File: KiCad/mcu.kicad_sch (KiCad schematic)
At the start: 12 parts, among them U6 STM32G0B1RET6, U7 RN4871-I_RM128, Y1 32.768kHz, Y2 8MHz

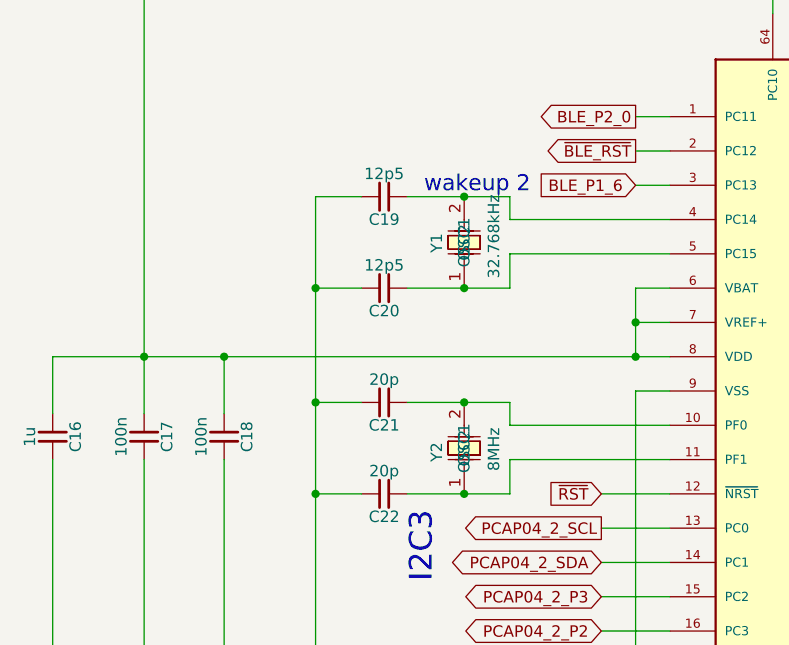
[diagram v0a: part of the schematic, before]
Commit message: crystal capacitors changed to correct values
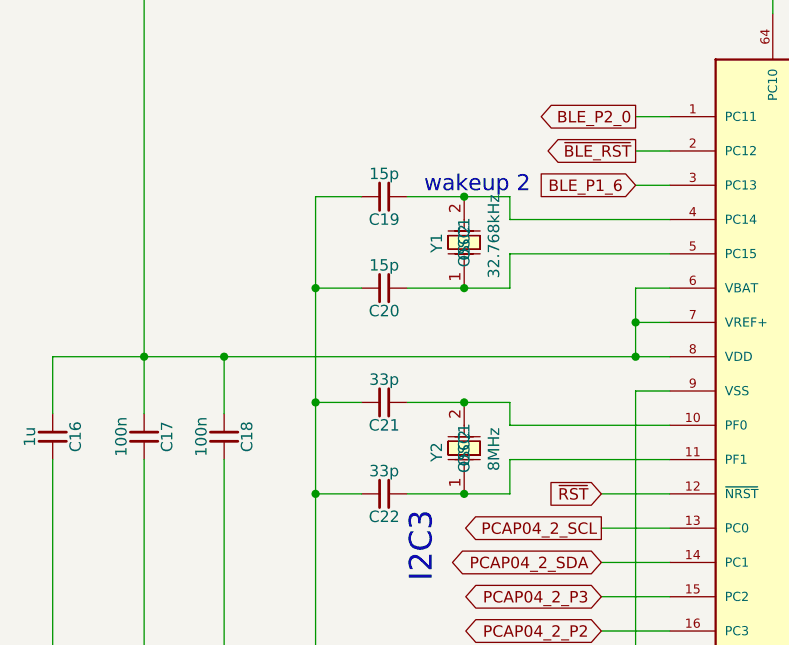
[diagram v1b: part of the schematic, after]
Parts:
- C19, C20: value 12p5 -> 15p; symbol sldrnrd:Capacitor/C0603_12p5 -> sldrnrd:Capacitor/C0603_15p; LCSC (none) -> C1644; MPN (none) -> CL10C150JB8NNNC; Manufacturer (none) -> Samsung Electro-Mechanics
- C21, C22: value 20p -> 33p; symbol sldrnrd:Capacitor/C0603_20p -> sldrnrd:Capacitor/C0603_33p; LCSC C1648 -> C1663; MPN CL10C200JB8NNNC -> CL10C330JB8NNNC; Manufacturer Samsung -> Samsung Electro-Mechanics
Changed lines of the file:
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@@
 	)
 	(symbol
-		(lib_id "sldrnrd:Capacitor/C0603_20p")
+		(lib_id "sldrnrd:Capacitor/C0603_33p")
 		(at 88.9 139.7 270)
 		(unit 1)
@@
 			)
 		)
-		(property "Value" "20p"
+		(property "Value" "33p"
 			(at 88.9 137.16 90)
 			(show_name no)
@@
 			)
 		)
-		(property "Description" "20pF Capacitor, 0603"
+		(property "Description" "33pF Capacitor, 0603"
 			(at 88.9 139.7 0)
 			(hide yes)
@@
 			)
 		)
-		(property "LCSC" "C1648"
+		(property "LCSC" "C1663"
 			(at 88.9 139.7 0)
 			(hide yes)
@@
 			)
 		)
-		(property "Manufacturer" "Samsung"
+		(property "Manufacturer" "Samsung Electro-Mechanics"
 			(at 88.9 139.7 0)
 			(hide yes)
@@
 			)
 		)
-		(property "MPN" "CL10C200JB8NNNC"
+		(property "MPN" "CL10C330JB8NNNC"
 			(at 88.9 139.7 0)
 			(hide yes)
@@
 	)
 	(symbol
-		(lib_id "sldrnrd:Capacitor/C0603_12p5")
+		(lib_id "sldrnrd:Capacitor/C0603_15p")
 		(at 88.9 106.68 270)
 		(unit 1)
@@
 			)
 		)
-		(property "Value" "12p5"
+		(property "Value" "15p"
 			(at 88.9 104.14 90)
 			(show_name no)
@@
 			)
 		)
-		(property "Description" "12.5pF Capacitor, 0603"
+		(property "Description" "15pF Capacitor, 0603"
 			(at 88.9 106.68 0)
 			(hide yes)
@@
 		)
 		(property "Voltage" "50V"
+			(at 88.9 106.68 0)
+			(hide yes)
+			(show_name no)
+			(do_not_autoplace no)
+			(effects
+				(font
+					(size 1.27 1.27)
+				)
+			)
+		)
+		(property "LCSC" "C1644"
+			(at 88.9 106.68 0)
+			(hide yes)
+			(show_name no)
+			(do_not_autoplace no)
+			(effects
+				(font
+					(size 1.27 1.27)
+				)
+			)
+		)
+		(property "Manufacturer" "Samsung Electro-Mechanics"
+			(at 88.9 106.68 0)
+			(hide yes)
+			(show_name no)
+			(do_not_autoplace no)
+			(effects
+				(font
+					(size 1.27 1.27)
+				)
+			)
+		)
+		(property "MPN" "CL10C150JB8NNNC"
 			(at 88.9 106.68 0)
 			(hide yes)
@@
 	)
 	(symbol
-		(lib_id "sldrnrd:Capacitor/C0603_12p5")
+		(lib_id "sldrnrd:Capacitor/C0603_15p")
 		(at 88.9 116.84 270)
 		(unit 1)
@@
 			)
 		)
-		(property "Value" "12p5"
+		(property "Value" "15p"
 			(at 88.9 114.3 90)
 			(show_name no)
@@
 			)
 		)
-		(property "Description" "12.5pF Capacitor, 0603"
+		(property "Description" "15pF Capacitor, 0603"
 			(at 88.9 116.84 0)
 			(hide yes)
@@
 		)
 		(property "Voltage" "50V"
+			(at 88.9 116.84 0)
+			(hide yes)
+			(show_name no)
+			(do_not_autoplace no)
+			(effects
+				(font
+					(size 1.27 1.27)
+				)
+			)
+		)
+		(property "LCSC" "C1644"
+			(at 88.9 116.84 0)
+			(hide yes)
+			(show_name no)
+			(do_not_autoplace no)
+			(effects
+				(font
+					(size 1.27 1.27)
+				)
+			)
+		)
+		(property "Manufacturer" "Samsung Electro-Mechanics"
+			(at 88.9 116.84 0)
+			(hide yes)
+			(show_name no)
+			(do_not_autoplace no)
+			(effects
+				(font
+					(size 1.27 1.27)
+				)
+			)
+		)
+		(property "MPN" "CL10C150JB8NNNC"
 			(at 88.9 116.84 0)
 			(hide yes)
@@
 	)
 	(symbol
-		(lib_id "sldrnrd:Capacitor/C0603_20p")
+		(lib_id "sldrnrd:Capacitor/C0603_33p")
 		(at 88.9 129.54 270)
 		(unit 1)
@@
 			)
 		)
-		(property "Value" "20p"
+		(property "Value" "33p"
 			(at 88.9 127 90)
 			(show_name no)
@@
 			)
 		)
-		(property "Description" "20pF Capacitor, 0603"
+		(property "Description" "33pF Capacitor, 0603"
 			(at 88.9 129.54 0)
 			(hide yes)
@@
 			)
 		)
-		(property "LCSC" "C1648"
+		(property "LCSC" "C1663"
 			(at 88.9 129.54 0)
 			(hide yes)
@@
 			)
 		)
-		(property "Manufacturer" "Samsung"
+		(property "Manufacturer" "Samsung Electro-Mechanics"
 			(at 88.9 129.54 0)
 			(hide yes)
@@
 			)
 		)
-		(property "MPN" "CL10C200JB8NNNC"
+		(property "MPN" "CL10C330JB8NNNC"
 			(at 88.9 129.54 0)
 			(hide yes)

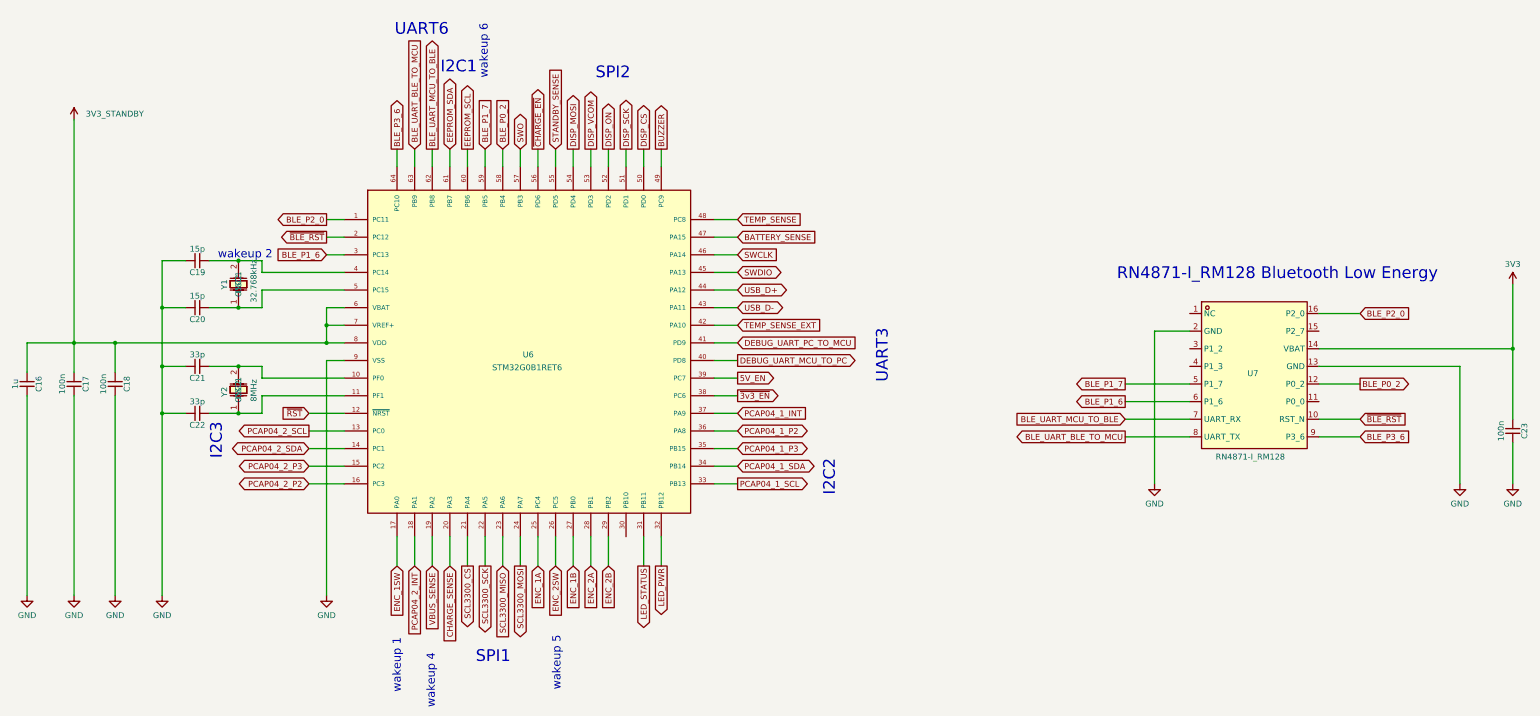
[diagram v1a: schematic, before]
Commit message: Symbols and board updated to match library
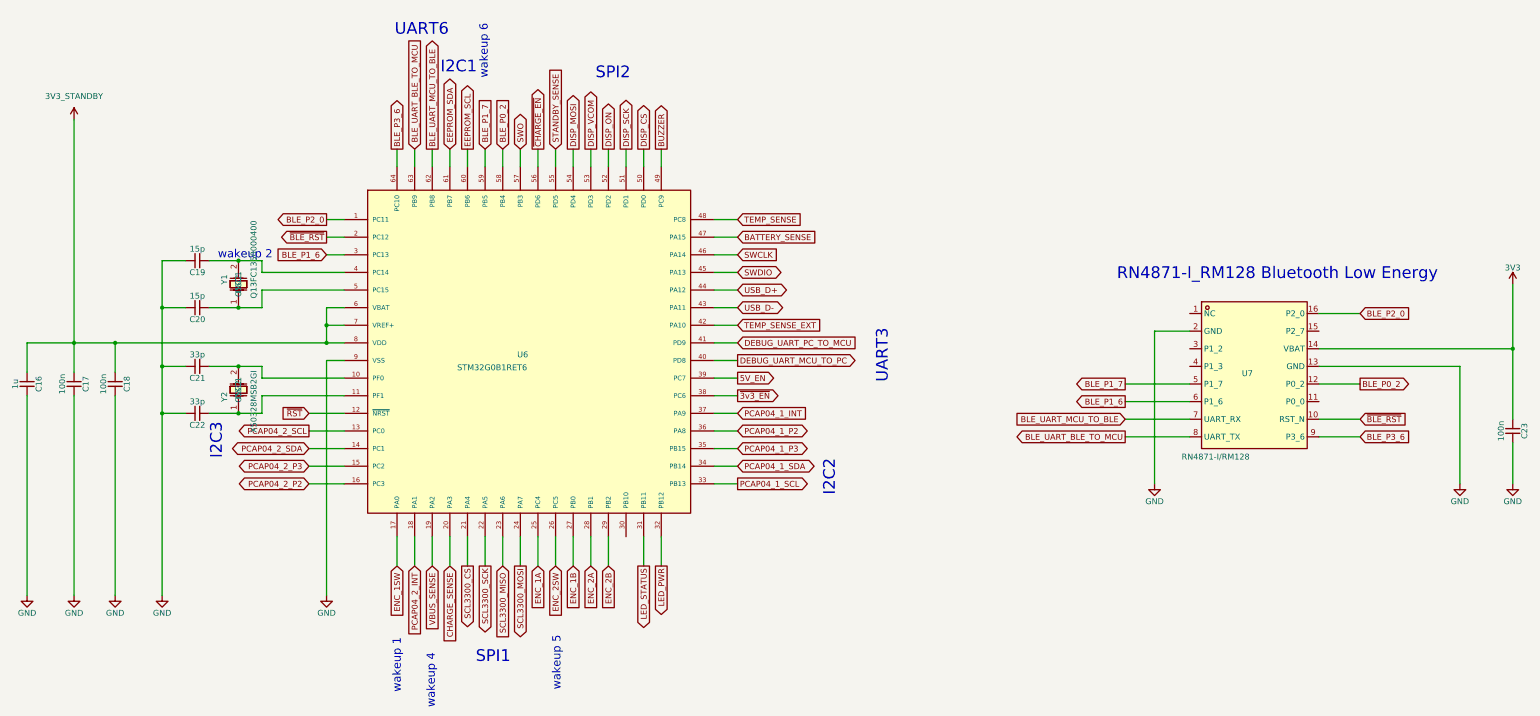
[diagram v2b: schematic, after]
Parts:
- U7: value RN4871-I_RM128 -> RN4871-I/RM128
- Y1: value 32.768kHz -> Q13FC1350000400
- Y2: value 8MHz -> X50328MSB2GI
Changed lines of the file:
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@@
 	)
 	(symbol
-		(lib_id "sldrnrd:Power/PWR/GND")
+		(lib_id "sldrnrd:PowerFlag/GND")
 		(at 62.23 179.07 0)
 		(unit 1)
@@
 		(in_pos_files yes)
 		(dnp no)
-		(property "Reference" "#PWR043"
+		(property "Reference" "#PWR43"
 			(at 62.23 185.42 0)
 			(hide yes)
@@
 		)
 		(property "Value" "GND"
-			(at 62.23 183.388 0)
+			(at 62.23 182.88 0)
 			(show_name no)
 			(do_not_autoplace no)
@@
 			)
 		)
-		(property "Datasheet" ""
+		(property "Datasheet" "~"
 			(at 62.23 179.07 0)
 			(hide yes)
@@
 			(project "InclinationMeter"
 				(path "/7d35597c-fbf9-4ce7-8410-0e7922679ea3/c7060150-8e88-4322-90f4-a2380d2eedad"
-					(reference "#PWR043")
+					(reference "#PWR43")
 					(unit 1)
 				)
@@
 					(size 1.27 1.27)
 				)
-				(justify left)
-			)
-		)
-		(property "Value" "RN4871-I_RM128"
+			)
+		)
+		(property "Value" "RN4871-I/RM128"
 			(at 309.118 149.098 0)
 			(show_name no)
@@
 					(size 1.27 1.27)
 				)
-				(justify left)
 			)
 		)
@@
 	)
 	(symbol
-		(lib_id "sldrnrd:Power/PWR/GND")
+		(lib_id "sldrnrd:PowerFlag/GND")
 		(at 71.12 179.07 0)
 		(unit 1)
@@
 		(in_pos_files yes)
 		(dnp no)
-		(property "Reference" "#PWR044"
+		(property "Reference" "#PWR44"
 			(at 71.12 185.42 0)
 			(hide yes)
@@
 		)
 		(property "Value" "GND"
-			(at 71.12 183.388 0)
+			(at 71.12 182.88 0)
 			(show_name no)
 			(do_not_autoplace no)
@@
 			)
 		)
-		(property "Datasheet" ""
+		(property "Datasheet" "~"
 			(at 71.12 179.07 0)
 			(hide yes)
@@
 			(project "InclinationMeter"
 				(path "/7d35597c-fbf9-4ce7-8410-0e7922679ea3/c7060150-8e88-4322-90f4-a2380d2eedad"
-					(reference "#PWR044")
+					(reference "#PWR44")
 					(unit 1)
 				)
@@
 	)
 	(symbol
-		(lib_id "sldrnrd:Power/PWR/GND")
+		(lib_id "sldrnrd:PowerFlag/GND")
 		(at 361.95 154.94 0)
 		(unit 1)
@@
 		(in_pos_files yes)
 		(dnp no)
-		(property "Reference" "#PWR048"
+		(property "Reference" "#PWR48"
 			(at 361.95 161.29 0)
 			(hide yes)
@@
 		)
 		(property "Value" "GND"
-			(at 361.95 159.258 0)
+			(at 361.95 158.75 0)
 			(show_name no)
 			(do_not_autoplace no)
@@
 			)
 		)
-		(property "Datasheet" ""
+		(property "Datasheet" "~"
 			(at 361.95 154.94 0)
 			(hide yes)
@@
 			(project "InclinationMeter"
 				(path "/7d35597c-fbf9-4ce7-8410-0e7922679ea3/c7060150-8e88-4322-90f4-a2380d2eedad"
-					(reference "#PWR048")
+					(reference "#PWR48")
 					(unit 1)
 				)
@@
 	)
 	(symbol
-		(lib_id "sldrnrd:Power/PWR/VCC")
+		(lib_id "sldrnrd:PowerFlag/3V3")
 		(at 62.23 76.2 0)
 		(unit 1)
@@
 		(dnp no)
 		(fields_autoplaced yes)
-		(property "Reference" "#PWR042"
+		(property "Reference" "#PWR42"
 			(at 62.23 80.01 0)
 			(hide yes)
@@
 		)
 		(property "Value" "3V3_STANDBY"
-			(at 64.77 74.9299 0)
-			(show_name no)
-			(do_not_autoplace no)
-			(effects
-				(font
-					(size 1.27 1.27)
-				)
-				(justify left)
+			(at 62.23 71.12 0)
+			(show_name no)
+			(do_not_autoplace no)
+			(effects
+				(font
+					(size 1.27 1.27)
+				)
 			)
 		)
@@
 			)
 		)
-		(property "Datasheet" ""
+		(property "Datasheet" "~"
 			(at 62.23 76.2 0)
 			(hide yes)
@@
 			)
 		)
-		(property "Description" "Power symbol creates a global label with name \"VCC\""
+		(property "Description" "Power symbol creates a global label with name \"3V3\", 3.3V supply"
 			(at 62.23 76.2 0)
 			(hide yes)
@@
 			(project "InclinationMeter"
 				(path "/7d35597c-fbf9-4ce7-8410-0e7922679ea3/c7060150-8e88-4322-90f4-a2380d2eedad"
-					(reference "#PWR042")
+					(reference "#PWR42")
 					(unit 1)
 				)
@@
 	)
 	(symbol
-		(lib_id "sldrnrd:Power/PWR/GND")
+		(lib_id "sldrnrd:PowerFlag/GND")
 		(at 81.28 179.07 0)
 		(unit 1)
@@
 		(in_pos_files yes)
 		(dnp no)
-		(property "Reference" "#PWR045"
+		(property "Reference" "#PWR45"
 			(at 81.28 185.42 0)
 			(hide yes)
@@
 		)
 		(property "Value" "GND"
-			(at 81.28 183.388 0)
+			(at 81.28 182.88 0)
 			(show_name no)
 			(do_not_autoplace no)
@@
 			)
 		)
-		(property "Datasheet" ""
+		(property "Datasheet" "~"
 			(at 81.28 179.07 0)
 			(hide yes)
@@
 			(project "InclinationMeter"
 				(path "/7d35597c-fbf9-4ce7-8410-0e7922679ea3/c7060150-8e88-4322-90f4-a2380d2eedad"
-					(reference "#PWR045")
+					(reference "#PWR45")
 					(unit 1)
 				)
@@
 	)
 	(symbol
-		(lib_id "sldrnrd:Power/PWR/GND")
+		(lib_id "sldrnrd:PowerFlag/GND")
 		(at 295.91 154.94 0)
 		(unit 1)
@@
 		(in_pos_files yes)
 		(dnp no)
-		(property "Reference" "#PWR047"
+		(property "Reference" "#PWR47"
 			(at 295.91 161.29 0)
 			(hide yes)
@@
 		)
 		(property "Value" "GND"
-			(at 295.91 159.258 0)
+			(at 295.91 158.75 0)
 			(show_name no)
 			(do_not_autoplace no)
@@
 			)
 		)
-		(property "Datasheet" ""
+		(property "Datasheet" "~"
 			(at 295.91 154.94 0)
 			(hide yes)
@@
 			(project "InclinationMeter"
 				(path "/7d35597c-fbf9-4ce7-8410-0e7922679ea3/c7060150-8e88-4322-90f4-a2380d2eedad"
-					(reference "#PWR047")
+					(reference "#PWR47")
 					(unit 1)
 				)
@@
 					(size 1.27 1.27)
 				)
-				(justify left)
 			)
 		)
@@
 					(size 1.27 1.27)
 				)
-				(justify left)
 			)
 		)
@@
 	)
 	(symbol
-		(lib_id "sldrnrd:Power/PWR/3V3")
+		(lib_id "sldrnrd:PowerFlag/3V3")
 		(at 373.38 111.76 0)
 		(unit 1)
@@
 		(in_pos_files yes)
 		(dnp no)
-		(property "Reference" "#PWR049"
+		(property "Reference" "#PWR49"
 			(at 373.38 115.57 0)
 			(hide yes)
@@
 		)
 		(property "Value" "3V3"
-			(at 373.38 107.442 0)
+			(at 373.38 108.204 0)
 			(show_name no)
 			(do_not_autoplace no)
@@
 			)
 		)
-		(property "Datasheet" ""
+		(property "Datasheet" "~"
 			(at 373.38 111.76 0)
 			(hide yes)
@@
 			(project "InclinationMeter"
 				(path "/7d35597c-fbf9-4ce7-8410-0e7922679ea3/c7060150-8e88-4322-90f4-a2380d2eedad"
-					(reference "#PWR049")
+					(reference "#PWR49")
 					(unit 1)
 				)
@@
 	)
 	(symbol
-		(lib_id "sldrnrd:Power/PWR/GND")
+		(lib_id "sldrnrd:PowerFlag/GND")
 		(at 52.07 179.07 0)
 		(unit 1)
@@
 		(in_pos_files yes)
 		(dnp no)
-		(property "Reference" "#PWR041"
+		(property "Reference" "#PWR41"
 			(at 52.07 185.42 0)
 			(hide yes)
@@
 		)
 		(property "Value" "GND"
-			(at 52.07 183.388 0)
+			(at 52.07 182.88 0)
 			(show_name no)
 			(do_not_autoplace no)
@@
 			)
 		)
-		(property "Datasheet" ""
+		(property "Datasheet" "~"
 			(at 52.07 179.07 0)
 			(hide yes)
@@
 			(project "InclinationMeter"
 				(path "/7d35597c-fbf9-4ce7-8410-0e7922679ea3/c7060150-8e88-4322-90f4-a2380d2eedad"
-					(reference "#PWR041")
+					(reference "#PWR41")
 					(unit 1)
 				)
@@
 					(size 1.27 1.27)
 				)
-				(justify left)
-			)
-		)
-		(property "Value" "8MHz"
+			)
+		)
+		(property "Value" "X50328MSB2GI"
 			(at 101.092 137.16 0)
 			(show_name no)
@@
 					(size 1.27 1.27)
 				)
-				(justify left)
 			)
 		)
@@
 	)
 	(symbol
-		(lib_id "sldrnrd:Power/PWR/GND")
+		(lib_id "sldrnrd:PowerFlag/GND")
 		(at 373.38 154.94 0)
 		(unit 1)
@@
 		(in_pos_files yes)
 		(dnp no)
-		(property "Reference" "#PWR050"
+		(property "Reference" "#PWR50"
 			(at 373.38 161.29 0)
 			(hide yes)
@@
 		)
 		(property "Value" "GND"
-			(at 373.38 159.258 0)
+			(at 373.38 158.75 0)
 			(show_name no)
 			(do_not_autoplace no)
@@
 			)
 		)
-		(property "Datasheet" ""
+		(property "Datasheet" "~"
 			(at 373.38 154.94 0)
 			(hide yes)
@@
 			(project "InclinationMeter"
 				(path "/7d35597c-fbf9-4ce7-8410-0e7922679ea3/c7060150-8e88-4322-90f4-a2380d2eedad"
-					(reference "#PWR050")
+					(reference "#PWR50")
 					(unit 1)
 				)
@@
 	)
 	(symbol
-		(lib_id "sldrnrd:Power/PWR/GND")
+		(lib_id "sldrnrd:PowerFlag/GND")
 		(at 116.84 179.07 0)
 		(unit 1)
@@
 		(in_pos_files yes)
 		(dnp no)
-		(property "Reference" "#PWR046"
+		(property "Reference" "#PWR46"
 			(at 116.84 185.42 0)
 			(hide yes)
@@
 		)
 		(property "Value" "GND"
-			(at 116.84 183.388 0)
+			(at 116.84 182.88 0)
 			(show_name no)
 			(do_not_autoplace no)
@@
 			)
 		)
-		(property "Datasheet" ""
+		(property "Datasheet" "~"
 			(at 116.84 179.07 0)
 			(hide yes)
@@
 			(project "InclinationMeter"
 				(path "/7d35597c-fbf9-4ce7-8410-0e7922679ea3/c7060150-8e88-4322-90f4-a2380d2eedad"
-					(reference "#PWR046")
+					(reference "#PWR46")
 					(unit 1)
 				)
@@
 					(size 1.27 1.27)
 				)
-				(justify right)
-			)
-		)
-		(property "Value" "32.768kHz"
+			)
+		)
+		(property "Value" "Q13FC1350000400"
 			(at 101.092 106.426 0)
 			(show_name no)
@@
 					(size 1.27 1.27)
 				)
-				(justify right)
-			)
-		)
+			)
+		)
